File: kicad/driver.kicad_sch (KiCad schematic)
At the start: 72 parts, among them Q1 IRFZ44NPBF, Q2 IRFZ44NPBF, Q3 IRFZ44NPBF, Q4 IRFZ44NPBF, Q5 IRFZ44NPBF, Q6 IRFZ44NPBF, U1 ir2104, U2 ir2104, U3 ir2104, U4 INA180A2IDBVR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

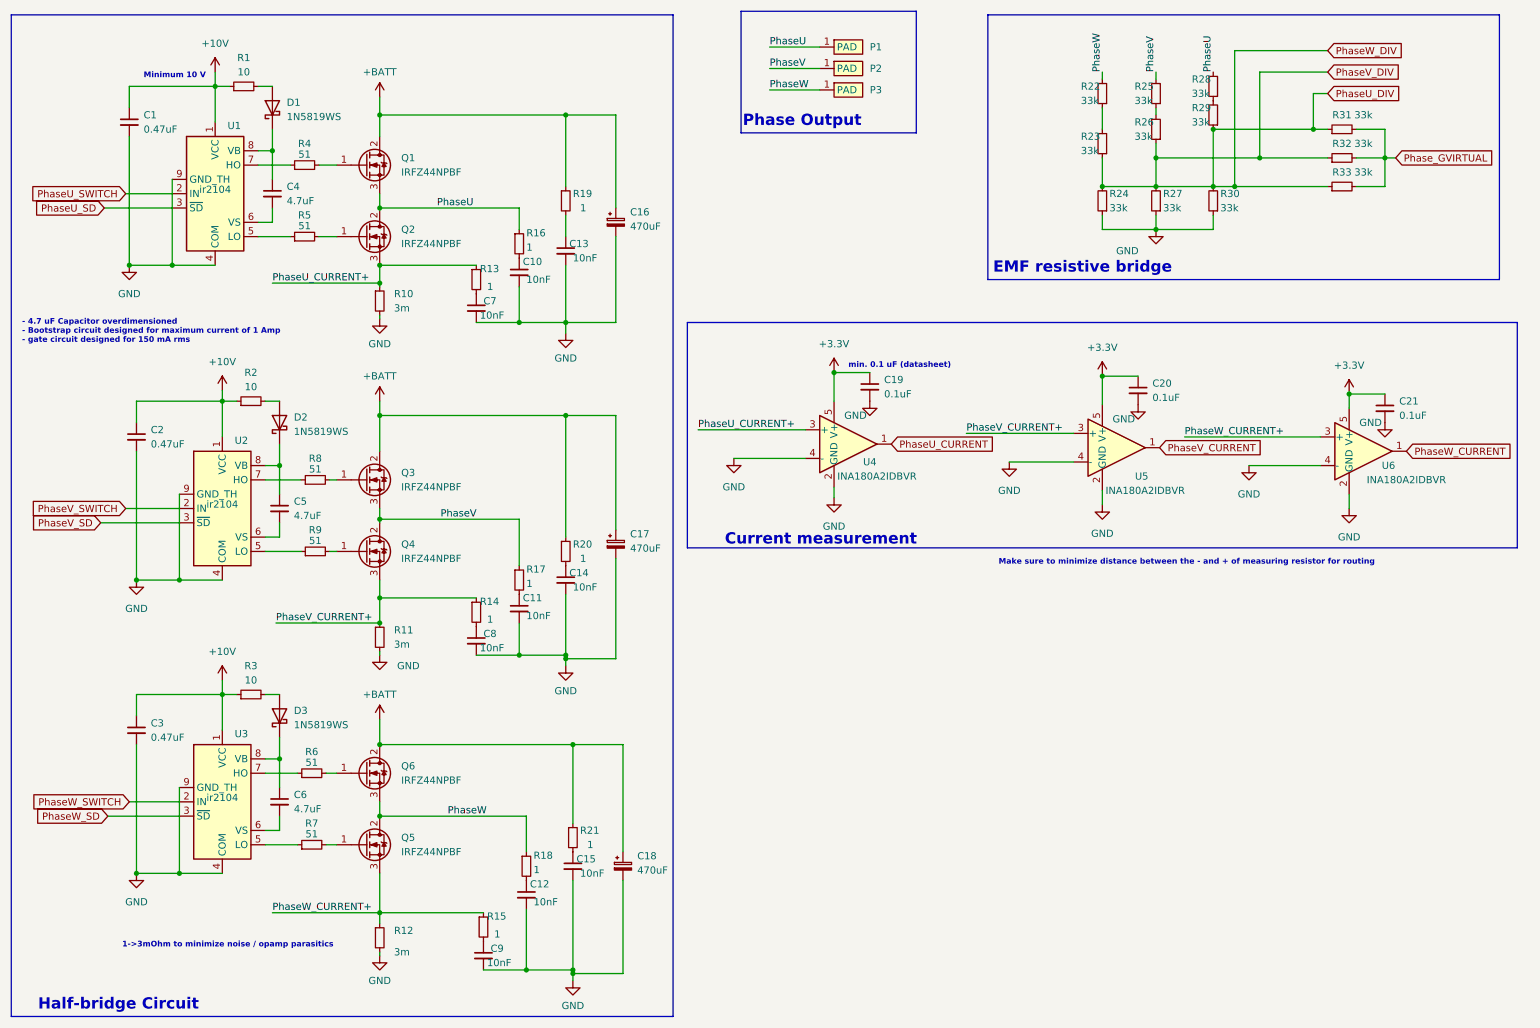
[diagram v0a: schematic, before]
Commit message: [kicad] Added testpoints, added 1 amp fuses at 2 buck converters
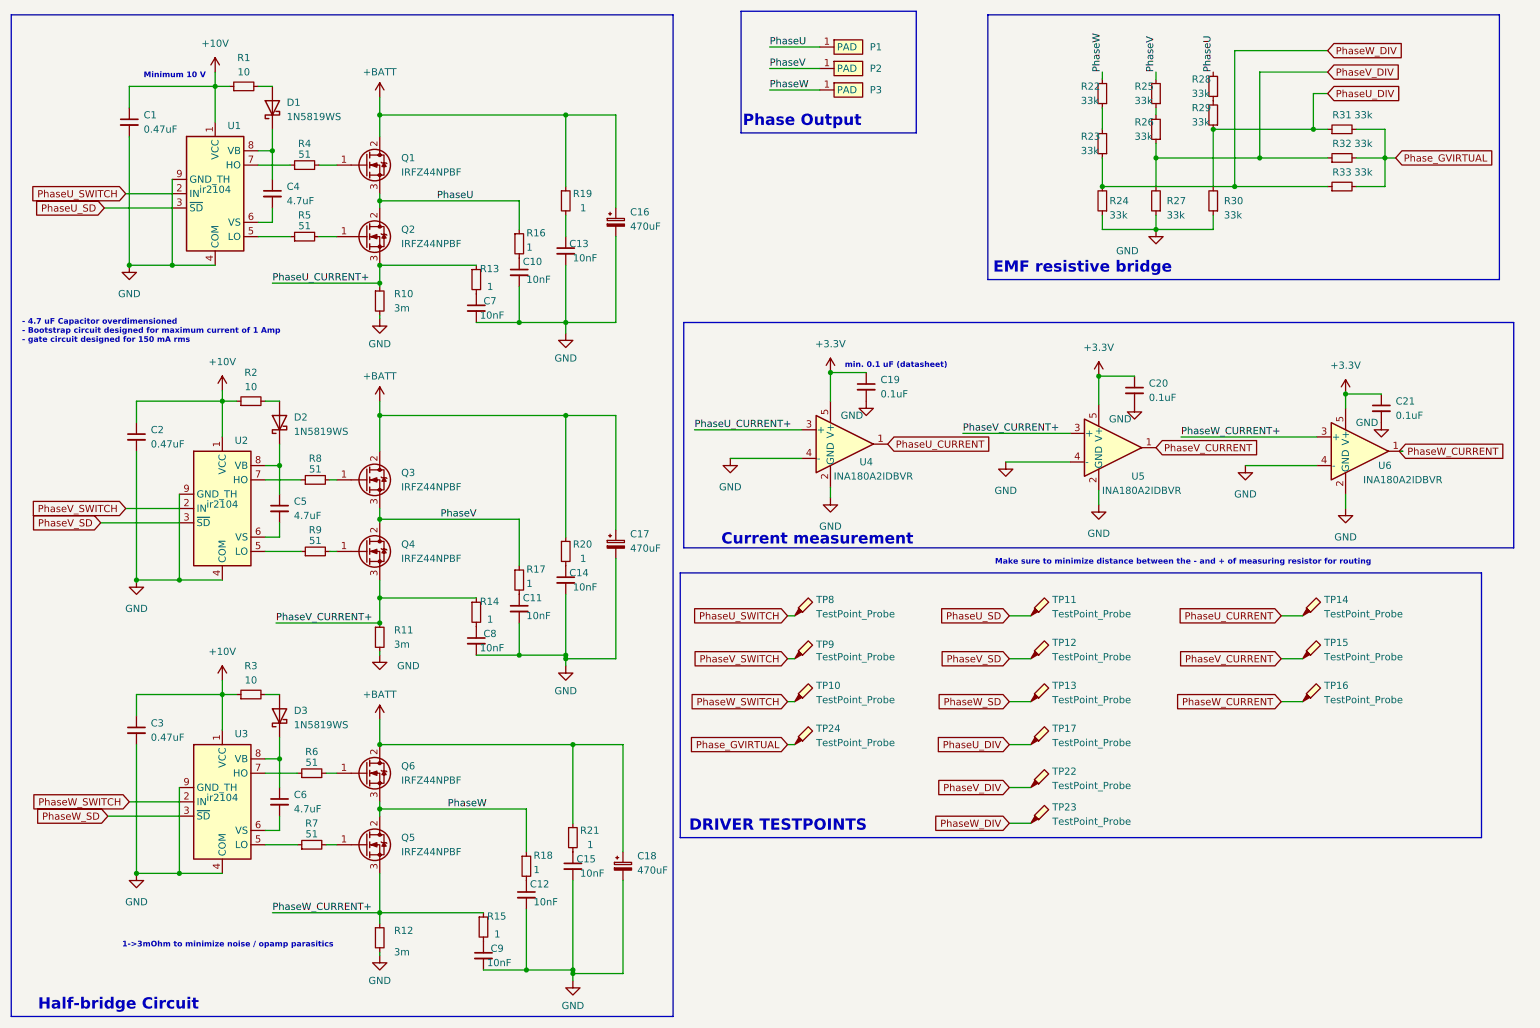
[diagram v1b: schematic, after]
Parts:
- added TP10, TP11, TP12, TP13, TP14, TP15, TP16, TP17, TP22, TP23, TP24, TP8, TP9: TestPoint_Probe, TestPoint:TestPoint_THTPad_D1.0mm_Drill0.5mm, symbol Connector:TestPoint_Probe
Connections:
- net PhaseU_CURRENT: now also TP14.1
- net PhaseU_DIV: now also TP17.1; no longer R23.1, R24.2, R26.1, R27.2, R32.1, R33.1
- net PhaseU_SD: now also TP11.1
- net PhaseU_SWITCH: now also TP8.1
- net PhaseV_CURRENT: now also TP15.1
- net PhaseV_SD: now also TP12.1
- net PhaseV_SWITCH: now also TP9.1
- net PhaseW_CURRENT: now also TP16.1
- net PhaseW_SD: now also TP13.1
- net PhaseW_SWITCH: now also TP10.1
- net Phase_GVIRTUAL: now also TP24.1
- new net PhaseV_DIV: R26.1, R27.2, R32.1, TP22.1
- new net PhaseW_DIV: R23.1, R24.2, R33.1, TP23.1
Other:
- moved on the sheet: C19, C20, C21, U4, U5, U6
